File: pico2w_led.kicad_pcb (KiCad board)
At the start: 2 copper layers, 21 x 51 mm, 17 parts, among them J1 Conn_01x20_MountingPin, J2 Conn_01x20_MountingPin, J3 Barrel_Jack, J4 Conn_01x04, U2 NTR3C21NZT3G, U3 NTR3C21NZT3G, U4 NTR3C21NZT3G, U5 AP62301WU-7

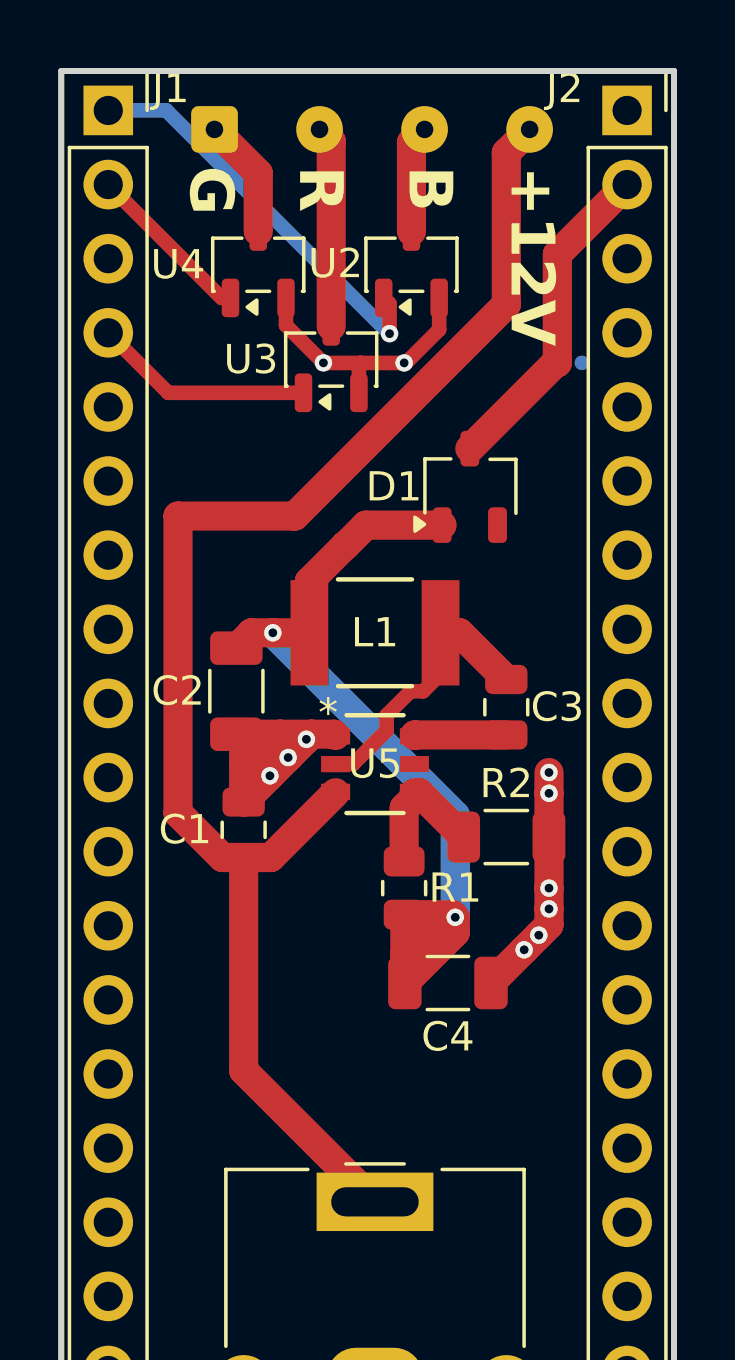
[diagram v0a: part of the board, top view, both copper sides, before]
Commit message: add bleed resistors
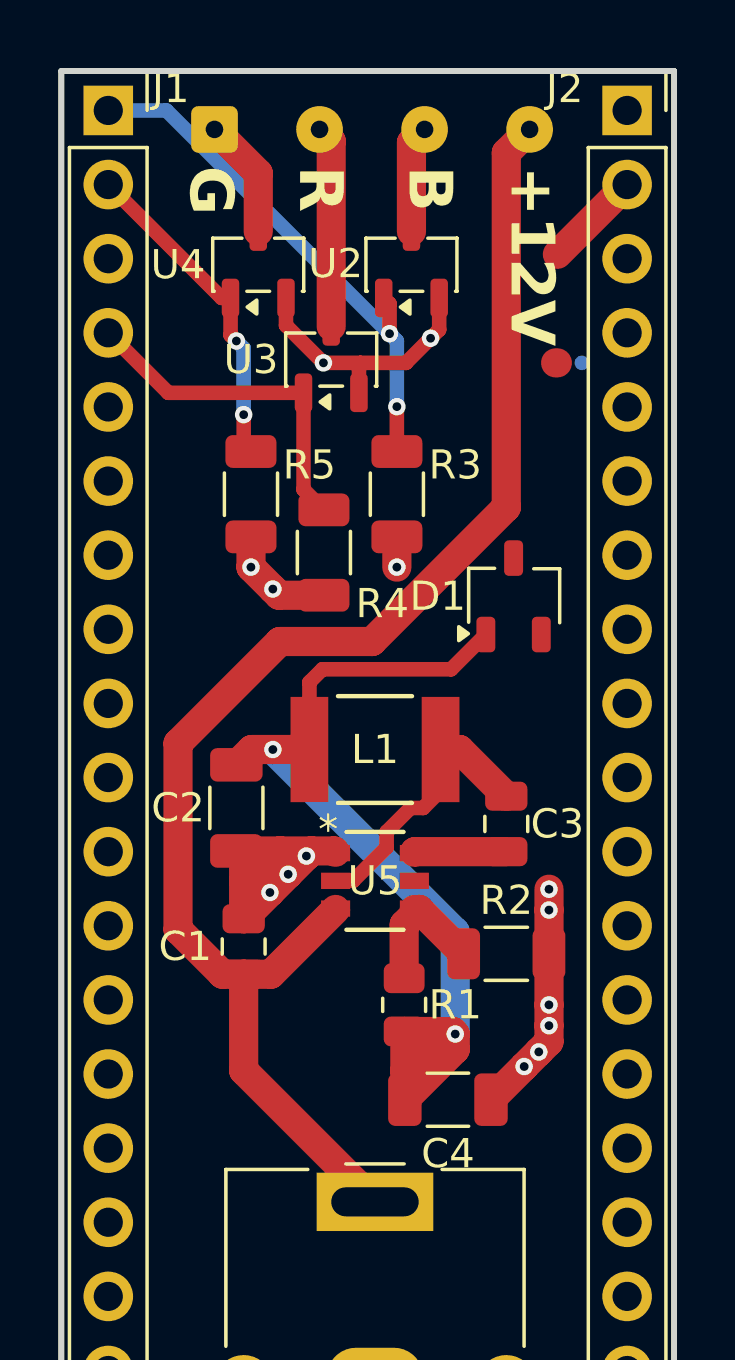
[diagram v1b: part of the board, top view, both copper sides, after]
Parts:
- added R3: 10k, Resistor_SMD:R_1206_3216Metric, F.Cu at (111.5, 64.5)
- added R4: 10k, Resistor_SMD:R_1206_3216Metric, F.Cu at (109.0, 66.5)
- added R5: 10k, Resistor_SMD:R_1206_3216Metric, F.Cu at (106.5, 64.5)
- moved D1 4.04 mm to (115.5, 68.0)
- moved C1 4.00 mm to (106.2, 80.0)
- moved C2 4.00 mm to (106.0, 75.2)
- moved C3 4.00 mm to (115.2, 75.8)
- moved C4 4.00 mm to (113.2, 85.2)
- moved L1 4.00 mm to (110.8, 73.2)
- moved R1 4.00 mm to (111.8, 82.0)
- moved R2 4.00 mm to (115.2, 80.2)
- moved U5 4.00 mm to (110.8, 77.8)
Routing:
- net /VSYS: track 11.3 -> 3.44 mm
- net /GPIO_01: track 5.80 -> 11.4 mm, vias 0 -> 2
- net GND: track 28.2 -> 33.1 mm, vias 11 -> 14
- net /GPIO_02: track 7.54 -> 11.8 mm
- net /B_GPIO: track 14.6 -> 18.7 mm, vias 1 -> 2
- net +5V: track 31.5 -> 33.4 mm

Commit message: Add screw terminal
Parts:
- added H1: MountingHole, MountingHole:MountingHole_2.2mm_M2, F.Cu at (2.48, 2.48)
- added H2: MountingHole, MountingHole:MountingHole_2.2mm_M2, F.Cu at (2.48, 8.43)
- added H3: MountingHole, MountingHole:MountingHole_2.2mm_M2, F.Cu at (2.48, 14.4)
- added H4: MountingHole, MountingHole:MountingHole_2.2mm_M2, F.Cu at (2.48, 20.3)
- added J5: Screw_Terminal_01x04, NTR3C21NZT3G:TBD05-04-1-G-G, F.Cu at (83.2, 51.2)
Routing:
- net /VSYS: track 3.44 -> 14.4 mm
